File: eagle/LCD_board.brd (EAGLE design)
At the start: 49 x 57 mm, 5 parts

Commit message: Second commit of Smart EVSE
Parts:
- added U$1: (no value), ohw-logo:OSHW_10X200_NOTEXT
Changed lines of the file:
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@@
 <setting verticaltext="up"/>
 </settings>
-<grid distance="0.05" unitdist="inch" unit="mm" style="lines" multiple="1" display="no" altdistance="0.1" altunitdist="mm" altunit="mm"/>
+<grid distance="0.05" unitdist="inch" unit="mil" style="lines" multiple="1" display="no" altdistance="3.937008" altunitdist="mil" altunit="mil"/>
 <layers>
 <layer number="1" name="Top" color="4" fill="1" visible="yes" active="yes"/>
@@
 <layer number="48" name="Document" color="7" fill="1" visible="no" active="yes"/>
 <layer number="49" name="Reference" color="7" fill="1" visible="no" active="yes"/>
+<layer number="50" name="dxf" color="7" fill="1" visible="no" active="no"/>
 <layer number="51" name="tDocu" color="7" fill="1" visible="no" active="yes"/>
 <layer number="52" name="bDocu" color="7" fill="1" visible="no" active="yes"/>
+<layer number="53" name="tGND_GNDA" color="7" fill="9" visible="no" active="no"/>
+<layer number="54" name="bGND_GNDA" color="1" fill="9" visible="no" active="no"/>
+<layer number="56" name="wert" color="7" fill="1" visible="no" active="yes"/>
 <layer number="91" name="Nets" color="2" fill="1" visible="no" active="no"/>
 <layer number="92" name="Busses" color="1" fill="1" visible="no" active="no"/>
@@
 <layer number="97" name="Info" color="7" fill="1" visible="no" active="no"/>
 <layer number="98" name="Guide" color="6" fill="1" visible="no" active="no"/>
+<layer number="100" name="Muster" color="7" fill="1" visible="no" active="no"/>
+<layer number="101" name="DRAWREF" color="11" fill="1" visible="no" active="yes"/>
+<layer number="102" name="Vscore" color="7" fill="1" visible="yes" active="yes"/>
+<layer number="103" name="tMap" color="7" fill="1" visible="yes" active="yes"/>
+<layer number="104" name="Name" color="16" fill="1" visible="yes" active="yes"/>
+<layer number="105" name="tPlate" color="7" fill="1" visible="yes" active="yes"/>
+<layer number="106" name="bPlate" color="7" fill="1" visible="yes" active="yes"/>
+<layer number="107" name="Crop" color="7" fill="1" visible="yes" active="yes"/>
+<layer number="116" name="Patch_BOT" color="9" fill="4" visible="yes" active="yes"/>
+<layer number="121" name="_tsilk" color="7" fill="1" visible="yes" active="yes"/>
+<layer number="122" name="_bsilk" color="7" fill="1" visible="yes" active="yes"/>
+<layer number="144" name="DrillLegend" color="7" fill="1" visible="no" active="yes"/>
+<layer number="151" name="HeatSink" color="7" fill="1" visible="yes" active="yes"/>
+<layer number="200" name="200bmp" color="1" fill="10" visible="no" active="yes"/>
+<layer number="201" name="201bmp" color="2" fill="10" visible="no" active="yes"/>
+<layer number="202" name="202bmp" color="3" fill="10" visible="no" active="yes"/>
+<layer number="203" name="203bmp" color="4" fill="10" visible="no" active="yes"/>
+<layer number="204" name="204bmp" color="5" fill="10" visible="no" active="yes"/>
+<layer number="205" name="205bmp" color="6" fill="10" visible="no" active="yes"/>
+<layer number="206" name="206bmp" color="7" fill="10" visible="no" active="yes"/>
+<layer number="207" name="207bmp" color="15" fill="10" visible="no" active="yes"/>
+<layer number="208" name="208bmp" color="9" fill="10" visible="yes" active="yes"/>
+<layer number="209" name="209bmp" color="7" fill="1" visible="yes" active="yes"/>
+<layer number="210" name="210bmp" color="7" fill="1" visible="yes" active="yes"/>
+<layer number="211" name="211bmp" color="7" fill="1" visible="yes" active="yes"/>
+<layer number="212" name="212bmp" color="7" fill="1" visible="yes" active="yes"/>
+<layer number="213" name="213bmp" color="7" fill="1" visible="yes" active="yes"/>
+<layer number="214" name="214bmp" color="7" fill="1" visible="yes" active="yes"/>
+<layer number="215" name="215bmp" color="7" fill="1" visible="yes" active="yes"/>
+<layer number="216" name="216bmp" color="7" fill="1" visible="yes" active="yes"/>
+<layer number="250" name="Descript" color="3" fill="1" visible="no" active="no"/>
+<layer number="251" name="SMDround" color="12" fill="11" visible="no" active="no"/>
+<layer number="254" name="cooling" color="7" fill="1" visible="yes" active="yes"/>
 </layers>
 <board>
@@
 <wire x1="0" y1="57" x2="0" y2="0" width="0" layer="20"/>
 <text x="15.9" y="10.97" size="1.016" layer="25" rot="R90">black</text>
-<text x="2.7" y="19.8" size="1.4224" layer="25" rot="R90">LCD8x2 Board v1.0</text>
+<text x="2.8" y="18.9" size="1.4224" layer="25" rot="R90">LCD8x2 Board v1.0</text>
 </plain>
 <attributes>
@@
 <param name="rvMicroViaOuter" value="0.25"/>
 <param name="rvMicroViaInner" value="0.25"/>
-<param name="rlMinPadTop" value="10mil"/>
+<param name="rlMinPadTop" value="12mil"/>
 <param name="rlMaxPadTop" value="20mil"/>
-<param name="rlMinPadInner" value="10mil"/>
+<param name="rlMinPadInner" value="12mil"/>
 <param name="rlMaxPadInner" value="20mil"/>
-<param name="rlMinPadBottom" value="10mil"/>
+<param name="rlMinPadBottom" value="12mil"/>
 <param name="rlMaxPadBottom" value="20mil"/>
-<param name="rlMinViaOuter" value="8mil"/>
+<param name="rlMinViaOuter" value="10mil"/>
 <param name="rlMaxViaOuter" value="20mil"/>
-<param name="rlMinViaInner" value="8mil"/>
+<param name="rlMinViaInner" value="10mil"/>
 <param name="rlMaxViaInner" value="20mil"/>
 <param name="rlMinMicroViaOuter" value="4mil"/>
@@
 </element>
 <element name="SJ1" library="jumper" package="SJ" value="" x="11.05" y="39.94" rot="MR90"/>
+<element name="U$1" library="ohw-logo" package="OSHW_10X200_NOTEXT" value="" x="38.1" y="11.43"/>
 </elements>
 <signals>
@@
 <contactref element="R1" pad="3"/>
 <contactref element="FTDI" pad="1"/>
-<polygon width="0" layer="16">
+<contactref element="SJ1" pad="2"/>
+<polygon width="0.4064" layer="16" isolate="0.4064">
 <vertex x="0" y="57.15"/>
-<vertex x="48.26" y="57.15"/>
-<vertex x="48.26" y="0"/>
+<vertex x="49.53" y="57.15"/>
+<vertex x="49.53" y="0"/>
 <vertex x="0" y="0"/>
 </polygon>
-<contactref element="SJ1" pad="2"/>
 </signal>
 <signal name="N$6">

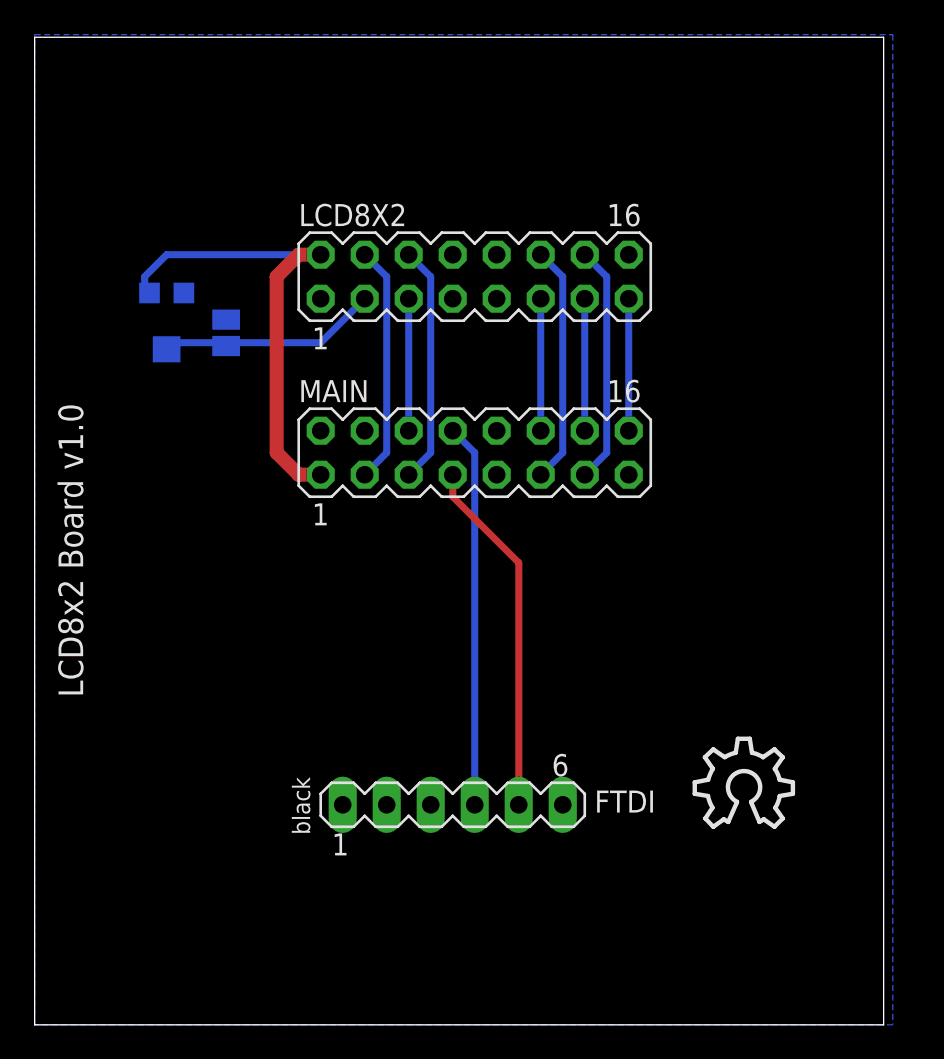
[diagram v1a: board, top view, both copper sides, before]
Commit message: version 1.05, LCD menu added
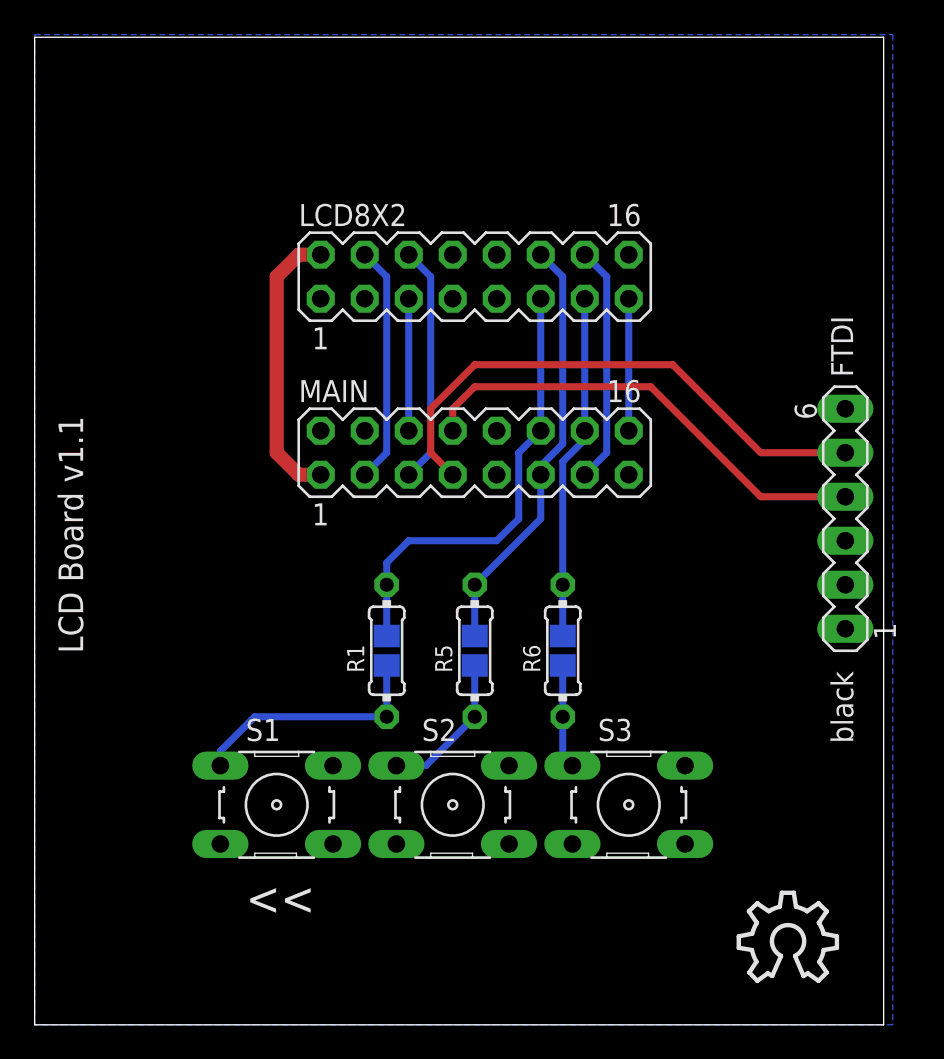
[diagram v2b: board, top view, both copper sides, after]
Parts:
- removed SJ1: (no value), jumper:SJ
- added R2, R3, R4: 470R, resistor:R0805
- added R5, R6: NP, resistor:0204/7
- added S1: <<, switch-omron:B3F-10XX
- added S2: Select, switch-omron:B3F-10XX
- added S3: >>, switch-omron:B3F-10XX
- R1: value 10KOHM -> NP; device Panasonic-Trimmer_Potentiometers:POT_EVM3W -> resistor:0204/7
- moved FTDI 28.0 mm to (46.8, 29.2), turned to 90 degrees
- moved R1 22.9 mm to (20.3, 21.6), flipped to the top, turned to 90 degrees
- moved U$1 9.25 mm to (40.6, 2.54)
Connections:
- removed net N$7: LCD8X2.3, R1.2, SJ1.1
- new net N$13: R1.1, R2.1, S1.1
- new net N$14: R3.1, R5.1, S2.1
- new net N$15: R4.1, R6.1, S3.1
- net GND: now also LCD8X2.3, S1.3, S1.4, S2.3, S2.4, S3.3, S3.4; no longer R1.3, SJ1.2
- net N$3: now also R4.2, R6.2
- net N$4: now also R1.2, R2.2
- net N$8: now also R3.2, R5.2
- net VCC: no longer R1.1
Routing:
- net N$4: track 7.62 -> 26.1 mm
- net N$13: track 0.00 -> 14.2 mm
- net N$7: track 12.8 -> 0.00 mm
- net N$3: track 7.62 -> 20.0 mm
- net VCC: track 28.0 -> 16.3 mm
- net N$8: track 13.8 -> 24.6 mm
- net N$1: track 20.6 -> 31.4 mm
- net N$14: track 0.00 -> 8.65 mm
- net N$15: track 0.00 -> 6.17 mm
- net N$12: track 22.1 -> 27.1 mm
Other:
- board text added: "LCD Board v1.1"
- board text removed: "LCD8x2 Board v1.0"
